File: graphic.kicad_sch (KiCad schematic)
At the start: 34 parts, among them P10 CONN_1, P11 CONN_1, P12 CONN_1, P4 CONN_2, P5 CONN_5, P9 CONN_1, U2 4C4001, U21 XC1736APD8, U23 XC4003/PQ100, U24 XC4005-PQ160, U7 AV9173, X1 10MHz

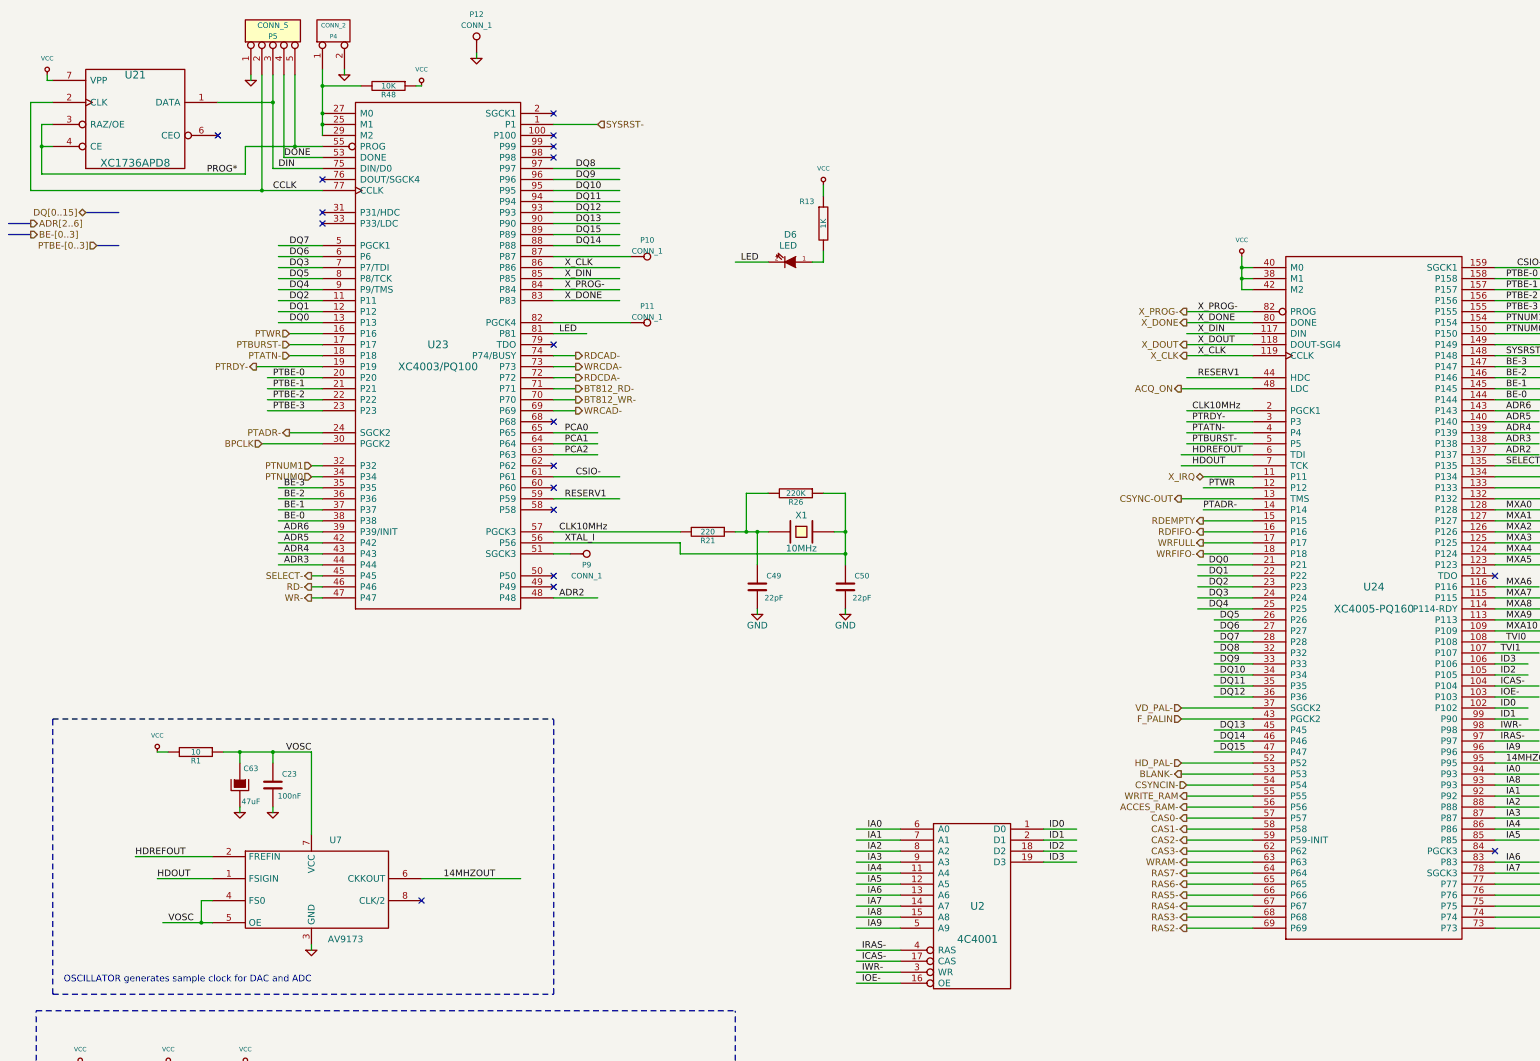
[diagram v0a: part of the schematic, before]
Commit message: update to kicad 9
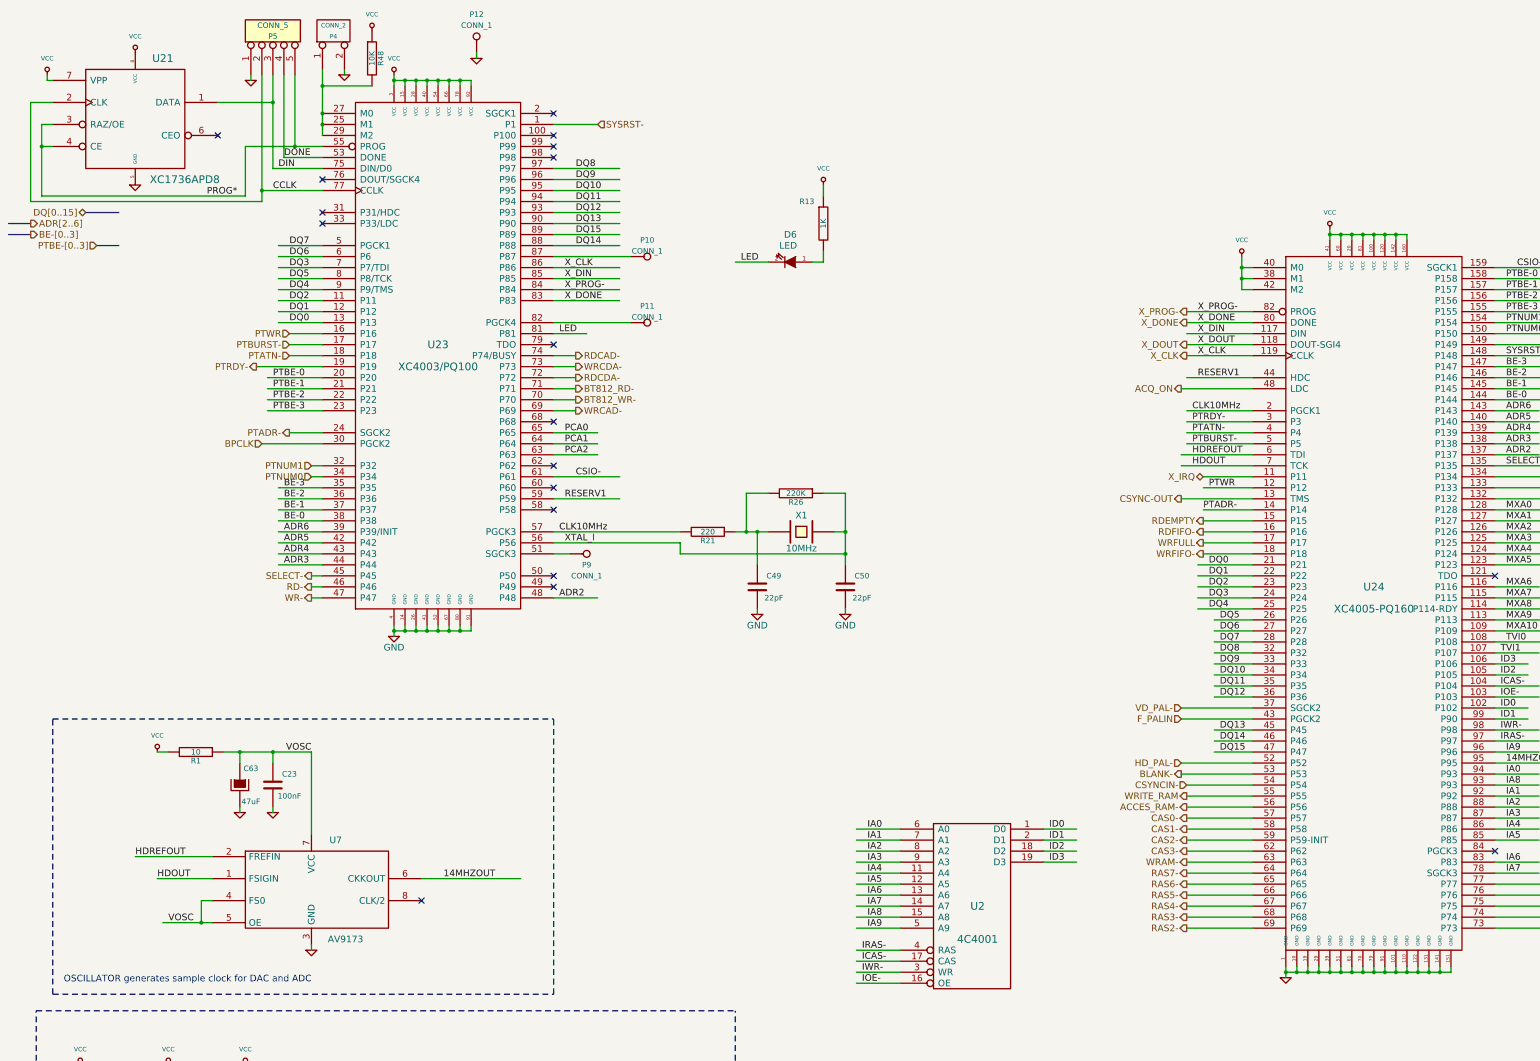
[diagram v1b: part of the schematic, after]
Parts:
- C17, C18, C19, C20, C21, C22, C23, C70, C71, C72, C73, R1, R13, R21, R26, R48: footprint Resistor_SMD:R_1206_3216Metric_Pad1.24x1.80mm_HandSolder -> Resistor_SMD:R_1206_3216Metric_Pad1.30x1.75mm_HandSolder
- C56, C57: footprint Capacitor_Tantalum_SMD:CP_EIA-3528-21_Kemet-B_Pad1.63x2.40mm_HandSolder -> Capacitor_Tantalum_SMD:CP_EIA-3528-21_Kemet-B_Pad1.50x2.35mm_HandSolder
- C63: footprint Resistor_SMD:R_1210_3225Metric_Pad1.24x2.70mm_HandSolder -> Resistor_SMD:R_1210_3225Metric_Pad1.30x2.65mm_HandSolder
- D6: footprint Discret:LEDV -> footprints:LED_D3.0mm
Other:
- moved on the sheet: R48
